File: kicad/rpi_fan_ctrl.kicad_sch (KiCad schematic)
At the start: 2 parts, among them J1 Conn_01x15_Socket

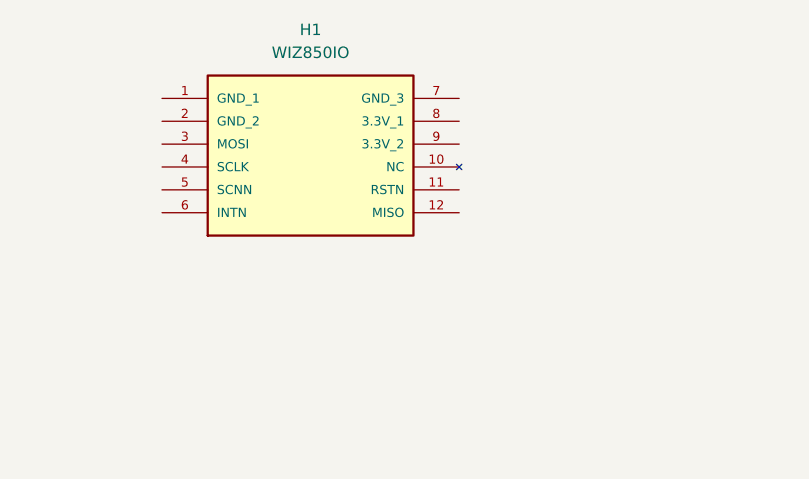
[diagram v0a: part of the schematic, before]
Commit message: w5500 ethernet schematic
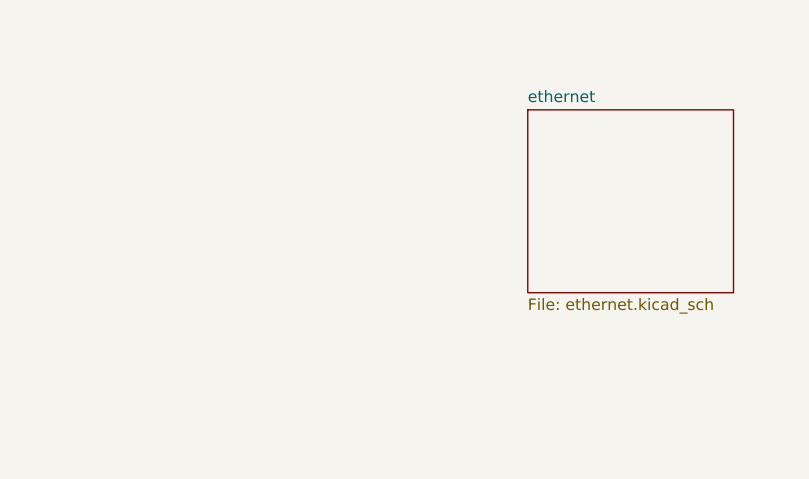
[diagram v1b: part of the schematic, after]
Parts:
- removed H1: WIZ850IO, WIZ850IO:WIZ850IO, symbol WIZ850IO:WIZ850IO
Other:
- added sheet ethernet (ethernet.kicad_sch)
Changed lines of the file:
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@@
-		)
-	)
-	(symbol
-		(lib_id "WIZ850IO:WIZ850IO")
-		(at 102.87 31.75 0)
-		(unit 1)
-		(exclude_from_sim no)
-		(in_bom yes)
-		(on_board yes)
-		(dnp no)
-		(fields_autoplaced yes)
-		(property "Reference" "H1"
-			(at 119.38 24.13 0)
-			(effects
-				(font
-					(size 1.27 1.27)
-				)
-			)
-		)
-		(property "Value" "WIZ850IO"
-			(at 119.38 26.67 0)
-			(effects
-				(font
-					(size 1.27 1.27)
-				)
-			)
-		)
-		(property "Footprint" "WIZ850IO:WIZ850IO"
-			(at 102.87 31.75 0)
-			(effects
-				(font
-					(size 1.27 1.27)
-				)
-				(justify bottom)
-				(hide yes)
-			)
-		)
-		(property "Datasheet" ""
-			(at 102.87 31.75 0)
-			(effects
-				(font
-					(size 1.27 1.27)
-				)
-				(hide yes)
-			)
-		)
-		(property "Description" ""
-			(at 102.87 31.75 0)
-			(effects
-				(font
-					(size 1.27 1.27)
-				)
-				(hide yes)
-			)
-		)
-		(property "MANUFACTURER_NAME" "Wiznet Technology"
-			(at 102.87 31.75 0)
-			(effects
-				(font
-					(size 1.27 1.27)
-				)
-				(justify bottom)
-				(hide yes)
-			)
-		)
-		(property "MF" "WIZnet"
-			(at 102.87 31.75 0)
-			(effects
-				(font
-					(size 1.27 1.27)
-				)
-				(justify bottom)
-				(hide yes)
-			)
-		)
-		(property "RS_PRICE-STOCK" ""
-			(at 102.87 31.75 0)
-			(effects
-				(font
-					(size 1.27 1.27)
-				)
-				(justify bottom)
-				(hide yes)
-			)
-		)
-		(property "DESCRIPTION" "WIZ820io network module that uses SPI and includes a W5500 and RJ45 jack with integrated transformer"
-			(at 102.87 31.75 0)
-			(effects
-				(font
-					(size 1.27 1.27)
-				)
-				(justify bottom)
-				(hide yes)
-			)
-		)
-		(property "RS_PART_NUMBER" ""
-			(at 102.87 31.75 0)
-			(effects
-				(font
-					(size 1.27 1.27)
-				)
-				(justify bottom)
-				(hide yes)
-			)
-		)
-		(property "Price" "None"
-			(at 102.87 31.75 0)
-			(effects
-				(font
-					(size 1.27 1.27)
-				)
-				(justify bottom)
-				(hide yes)
-			)
-		)
-		(property "Package" "Module WIZnet"
-			(at 102.87 31.75 0)
-			(effects
-				(font
-					(size 1.27 1.27)
-				)
-				(justify bottom)
-				(hide yes)
-			)
-		)
-		(property "Check_prices" "https://www.snapeda.com/parts/WIZ850IO/WIZnet/view-part/?ref=eda"
-			(at 102.87 31.75 0)
-			(effects
-				(font
-					(size 1.27 1.27)
-				)
-				(justify bottom)
-				(hide yes)
-			)
-		)
-		(property "HEIGHT" "17mm"
-			(at 102.87 31.75 0)
-			(effects
-				(font
-					(size 1.27 1.27)
-				)
-				(justify bottom)
-				(hide yes)
-			)
-		)
-		(property "MP" "WIZ850IO"
-			(at 102.87 31.75 0)
-			(effects
-				(font
-					(size 1.27 1.27)
-				)
-				(justify bottom)
-				(hide yes)
-			)
-		)
-		(property "SnapEDA_Link" "https://www.snapeda.com/parts/WIZ850IO/WIZnet/view-part/?ref=snap"
-			(at 102.87 31.75 0)
-			(effects
-				(font
-					(size 1.27 1.27)
-				)
-				(justify bottom)
-				(hide yes)
-			)
-		)
-		(property "ARROW_PRICE-STOCK" "https://www.arrow.com/en/products/wiz850io/wiznet"
-			(at 102.87 31.75 0)
-			(effects
-				(font
-					(size 1.27 1.27)
-				)
-				(justify bottom)
-				(hide yes)
-			)
-		)
-		(property "ARROW_PART_NUMBER" "WIZ850IO"
-			(at 102.87 31.75 0)
-			(effects
-				(font
-					(size 1.27 1.27)
-				)
-				(justify bottom)
-				(hide yes)
-			)
-		)
-		(property "Description_1" "Ethernet - 10/100 Base-T/TX PHY SPI Interface Module"
-			(at 102.87 31.75 0)
-			(effects
-				(font
-					(size 1.27 1.27)
-				)
-				(justify bottom)
-				(hide yes)
-			)
-		)
-		(property "Availability" "In Stock"
-			(at 102.87 31.75 0)
-			(effects
-				(font
-					(size 1.27 1.27)
-				)
-				(justify bottom)
-				(hide yes)
-			)
-		)
-		(property "MANUFACTURER_PART_NUMBER" "WIZ850IO"
-			(at 102.87 31.75 0)
-			(effects
-				(font
-					(size 1.27 1.27)
-				)
-				(justify bottom)
-				(hide yes)
-			)
-		)
-		(pin "2"
-		)
-		(pin "12"
-		)
-		(pin "4"
-		)
-		(pin "7"
-		)
-		(pin "8"
-		)
-		(pin "10"
-		)
-		(pin "9"
-		)
-		(pin "5"
-		)
-		(pin "6"
-		)
-		(pin "11"
-		)
-		(pin "3"
-		)
-		(pin "1"
-		)
-		(instances
-			(project ""
-				(path "/ea853fa5-7daa-4d53-920c-149f1dc74042"
-					(reference "H1")
-					(unit 1)
-				)
-			)
 		)
 	)
@@
 				)
 			)
+		)
+	)
+	(sheet
+		(at 143.51 33.02)
+		(size 22.86 20.32)
+		(exclude_from_sim no)
+		(in_bom yes)
+		(on_board yes)
+		(dnp no)
+		(fields_autoplaced yes)
+		(stroke
+			(width 0.1524)
+			(type solid)
+		)
+		(fill
+			(color 0 0 0 0.0000)
+		)
+		(property "Sheetname" "ethernet"
+			(at 143.51 32.3084 0)
+			(effects
+				(font
+					(size 1.27 1.27)
+				)
+				(justify left bottom)
+			)
+		)
+		(property "Sheetfile" "ethernet.kicad_sch"
+			(at 143.51 53.9246 0)
+			(effects
+				(font
+					(size 1.27 1.27)
+				)
+				(justify left top)
+			)
+		)
+		(instances
+			(project "rpi_fan_ctrl"
+				(path "/ea853fa5-7daa-4d53-920c-149f1dc74042"
+					(page "3")
+				)
+			)

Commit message: hierarchical sheet
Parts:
- removed J1: Conn_01x15_Socket, symbol Connector:Conn_01x15_Socket
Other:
- sheet ethernet ports: added 3.3V, GND, INTn, MISO, MOSI, RSTn, SCLK, SCSn; removed none
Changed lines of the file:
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@@
 	(generator_version "9.0")
 	(paper "A4")
-	(junction
-		(at 52.07 87.63)
-		(diameter 0)
-		(color 0 0 0 0)
-	)
-	(junction
-		(at 52.07 95.25)
-		(diameter 0)
-		(color 0 0 0 0)
-	)
-	(junction
-		(at 52.07 102.87)
-		(diameter 0)
-		(color 0 0 0 0)
-	)
-	(junction
-		(at 52.07 80.01)
-		(diameter 0)
-		(color 0 0 0 0)
-	)
-	(junction
-		(at 52.07 72.39)
-		(diameter 0)
-		(color 0 0 0 0)
-	)
-	(wire
-		(pts
-			(xy 52.07 80.01) (xy 52.07 82.55)
-		)
-		(stroke
-			(width 0)
-			(type default)
-		)
-	)
-	(wire
-		(pts
-			(xy 52.07 100.33) (xy 52.07 102.87)
-		)
-		(stroke
-			(width 0)
-			(type default)
-		)
-	)
-	(wire
-		(pts
-			(xy 52.07 92.71) (xy 52.07 95.25)
-		)
-		(stroke
-			(width 0)
-			(type default)
-		)
-	)
-	(wire
-		(pts
-			(xy 52.07 85.09) (xy 52.07 87.63)
-		)
-		(stroke
-			(width 0)
-			(type default)
-		)
-	)
-	(wire
-		(pts
-			(xy 52.07 102.87) (xy 52.07 105.41)
-		)
-		(stroke
-			(width 0)
-			(type default)
-		)
-	)
-	(wire
-		(pts
-			(xy 52.07 95.25) (xy 52.07 97.79)
-		)
-		(stroke
-			(width 0)
-			(type default)
-		)
-	)
-	(wire
-		(pts
-			(xy 52.07 72.39) (xy 52.07 74.93)
-		)
-		(stroke
-			(width 0)
-			(type default)
-		)
-	)
-	(wire
-		(pts
-			(xy 52.07 77.47) (xy 52.07 80.01)
-		)
-		(stroke
-			(width 0)
-			(type default)
-		)
-	)
-	(wire
-		(pts
-			(xy 52.07 87.63) (xy 52.07 90.17)
-		)
-		(stroke
-			(width 0)
-			(type default)
-		)
-	)
-	(wire
-		(pts
-			(xy 52.07 69.85) (xy 52.07 72.39)
-		)
-		(stroke
-			(width 0)
-			(type default)
-		)
-	)
-	(symbol
-		(lib_id "Connector:Conn_01x15_Socket")
-		(at 46.99 87.63 180)
-		(unit 1)
-		(exclude_from_sim no)
-		(in_bom yes)
-		(on_board yes)
-		(dnp no)
-		(fields_autoplaced yes)
-		(property "Reference" "J1"
-			(at 47.625 64.77 0)
-			(effects
-				(font
-					(size 1.27 1.27)
-				)
-			)
-		)
-		(property "Value" "Conn_01x15_Socket"
-			(at 47.625 67.31 0)
-			(effects
-				(font
-					(size 1.27 1.27)
-				)
-			)
-		)
-		(property "Footprint" ""
-			(at 46.99 87.63 0)
-			(effects
-				(font
-					(size 1.27 1.27)
-				)
-				(hide yes)
-			)
-		)
-		(property "Datasheet" "~"
-			(at 46.99 87.63 0)
-			(effects
-				(font
-					(size 1.27 1.27)
-				)
-				(hide yes)
-			)
-		)
-		(property "Description" "Generic connector, single row, 01x15, script generated"
-			(at 46.99 87.63 0)
-			(effects
-				(font
-					(size 1.27 1.27)
-				)
-				(hide yes)
-			)
-		)
-		(pin "12"
-		)
-		(pin "13"
-		)
-		(pin "4"
-		)
-		(pin "14"
-		)
-		(pin "10"
-		)
-		(pin "1"
-		)
-		(pin "3"
-		)
-		(pin "5"
-		)
-		(pin "7"
-		)
-		(pin "2"
-		)
-		(pin "15"
-		)
-		(pin "9"
-		)
-		(pin "8"
-		)
-		(pin "11"
-		)
-		(pin "6"
-		)
-		(instances
-			(project ""
-				(path "/ea853fa5-7daa-4d53-920c-149f1dc74042"
-					(reference "J1")
-					(unit 1)
-				)
-			)
-		)
-	)
 	(sheet
 		(at 146.05 81.28)
@@
 	)
 	(sheet
-		(at 143.51 33.02)
-		(size 22.86 20.32)
+		(at 147.32 41.656)
+		(size 19.812 19.304)
 		(exclude_from_sim no)
 		(in_bom yes)
@@
 		)
 		(property "Sheetname" "ethernet"
-			(at 143.51 32.3084 0)
+			(at 147.32 40.9444 0)
 			(effects
 				(font
@@
 		)
 		(property "Sheetfile" "ethernet.kicad_sch"
-			(at 143.51 53.9246 0)
+			(at 147.32 61.5446 0)
 			(effects
 				(font
@@
 			)
 		)
+		(pin "3.3V" passive
+			(at 147.32 49.53 180)
+			(effects
+				(font
+					(size 1.27 1.27)
+				)
+				(justify left)
+			)
+		)
+		(pin "GND" passive
+			(at 147.32 52.07 180)
+			(effects
+				(font
+					(size 1.27 1.27)
+				)
+				(justify left)
+			)
+		)
+		(pin "INTn" input
+			(at 167.132 52.07 0)
+			(effects
+				(font
+					(size 1.27 1.27)
+				)
+				(justify right)
+			)
+		)
+		(pin "MISO" output
+			(at 161.29 60.96 270)
+			(effects
+				(font
+					(size 1.27 1.27)
+				)
+				(justify left)
+			)
+		)
+		(pin "MOSI" input
+			(at 153.67 60.96 270)
+			(effects
+				(font
+					(size 1.27 1.27)
+				)
+				(justify left)
+			)
+		)
+		(pin "RSTn" input
+			(at 167.132 49.53 0)
+			(effects
+				(font
+					(size 1.27 1.27)
+				)
+				(justify right)
+			)
+		)
+		(pin "SCLK" input
+			(at 156.21 60.96 270)
+			(effects
+				(font
+					(size 1.27 1.27)
+				)
+				(justify left)
+			)
+		)
+		(pin "SCSn" input
+			(at 158.75 60.96 270)
+			(effects
+				(font
+					(size 1.27 1.27)
+				)
+				(justify left)
+			)
+		)

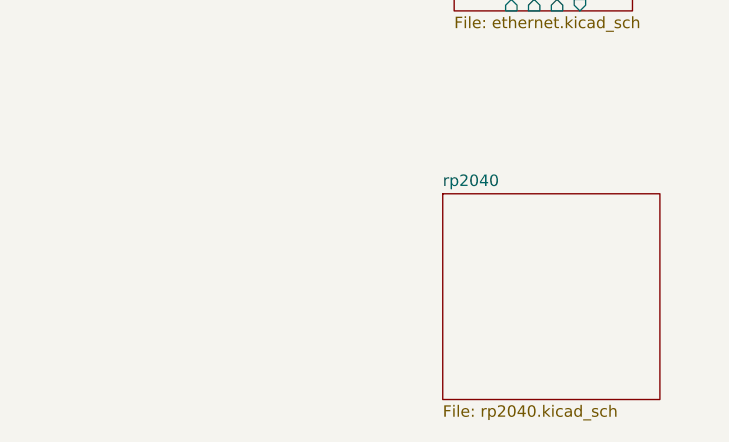
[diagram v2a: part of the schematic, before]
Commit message: power input schematic
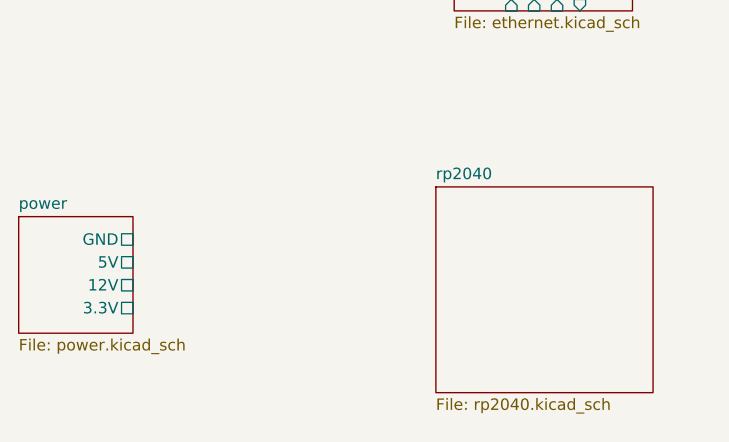
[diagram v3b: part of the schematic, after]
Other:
- added sheet power (power.kicad_sch)
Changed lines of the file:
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@@
 	(paper "A4")
 	(sheet
-		(at 146.05 81.28)
+		(at 98.933 83.82)
+		(size 12.7 12.954)
+		(exclude_from_sim no)
+		(in_bom yes)
+		(on_board yes)
+		(dnp no)
+		(fields_autoplaced yes)
+		(stroke
+			(width 0.1524)
+			(type solid)
+		)
+		(fill
+			(color 0 0 0 0.0000)
+		)
+		(property "Sheetname" "power"
+			(at 98.933 83.1084 0)
+			(effects
+				(font
+					(size 1.27 1.27)
+				)
+				(justify left bottom)
+			)
+		)
+		(property "Sheetfile" "power.kicad_sch"
+			(at 98.933 97.3586 0)
+			(effects
+				(font
+					(size 1.27 1.27)
+				)
+				(justify left top)
+			)
+		)
+		(pin "3.3V" passive
+			(at 111.633 93.98 0)
+			(effects
+				(font
+					(size 1.27 1.27)
+				)
+				(justify right)
+			)
+		)
+		(pin "5V" passive
+			(at 111.633 88.9 0)
+			(effects
+				(font
+					(size 1.27 1.27)
+				)
+				(justify right)
+			)
+		)
+		(pin "12V" passive
+			(at 111.633 91.44 0)
+			(effects
+				(font
+					(size 1.27 1.27)
+				)
+				(justify right)
+			)
+		)
+		(pin "GND" passive
+			(at 111.633 86.36 0)
+			(effects
+				(font
+					(size 1.27 1.27)
+				)
+				(justify right)
+			)
+		)
+		(instances
+			(project "rpi_fan_ctrl"
+				(path "/ea853fa5-7daa-4d53-920c-149f1dc74042"
+					(page "4")
+				)
+			)
+		)
+	)
+	(sheet
+		(at 145.288 80.518)
 		(size 24.13 22.86)
 		(exclude_from_sim no)
@@
 		)
 		(property "Sheetname" "rp2040"
-			(at 146.05 80.5684 0)
+			(at 145.288 79.8064 0)
 			(effects
 				(font
@@
 		)
 		(property "Sheetfile" "rp2040.kicad_sch"
-			(at 146.05 104.7246 0)
+			(at 145.288 103.9626 0)
 			(effects
 				(font

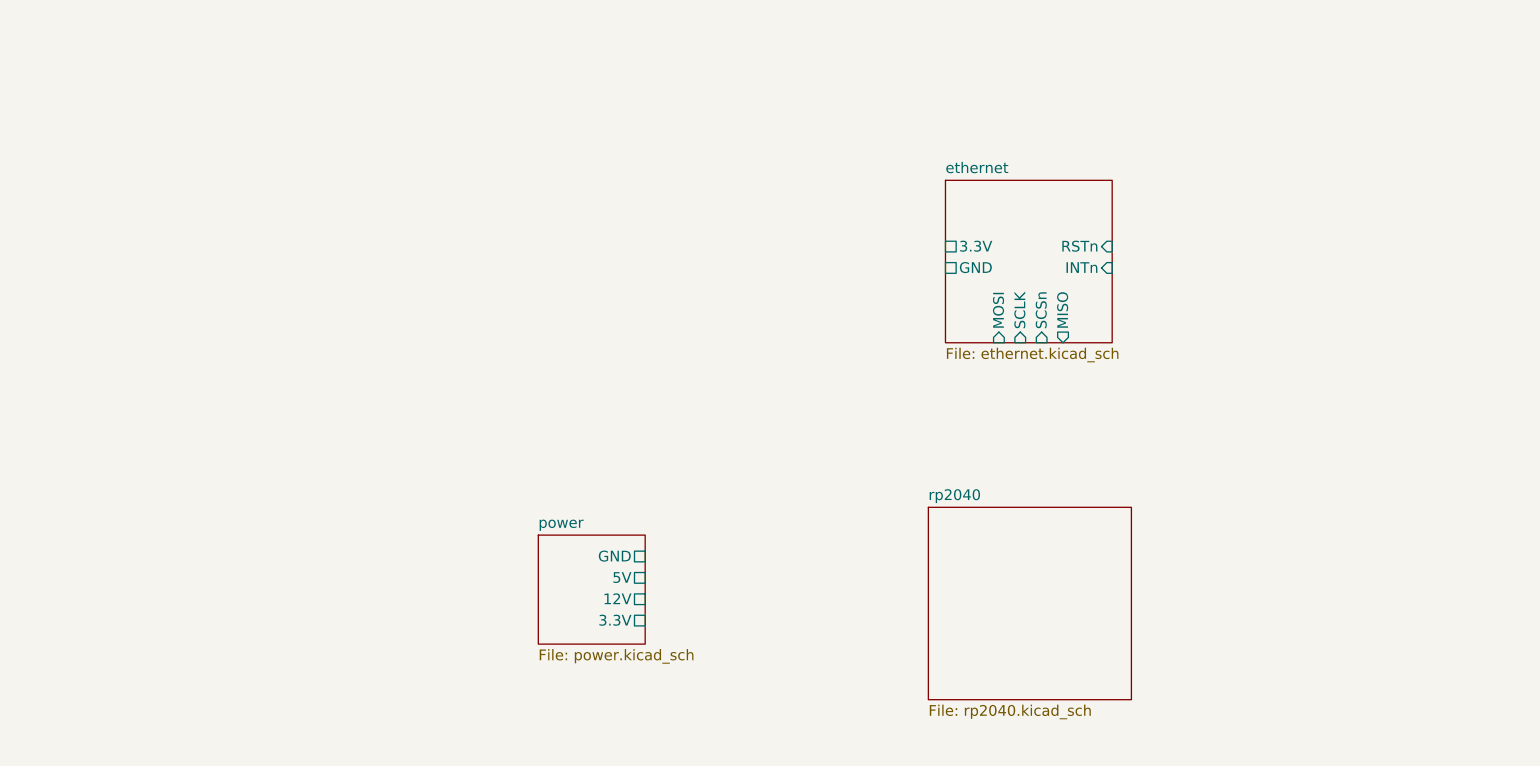
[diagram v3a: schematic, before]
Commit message: finished circuits for rp2040
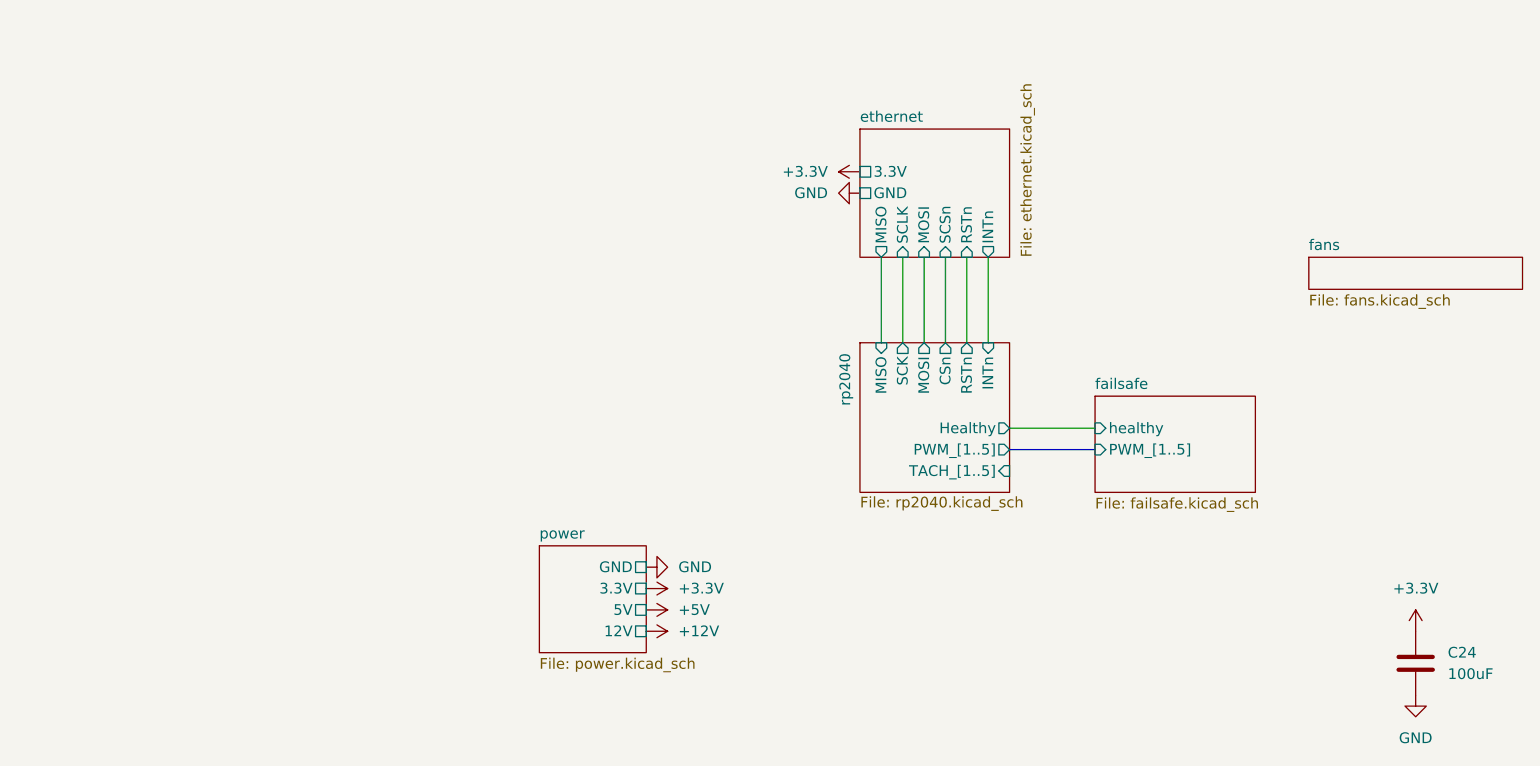
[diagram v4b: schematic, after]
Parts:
- added C24: 100uF, symbol Device:C
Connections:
- new net +3.3V: C24.1
- new net GND: C24.2
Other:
- added sheet failsafe (failsafe.kicad_sch)
- added sheet fans (fans.kicad_sch)
- sheet rp2040 ports: added CSn, Healthy, INTn, MISO, MOSI, PWM_[1..5], RSTn, SCK, TACH_[1..5]; removed none
